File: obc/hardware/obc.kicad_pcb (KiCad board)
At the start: 4 copper layers, 80 x 80 mm, 88 parts, among them J1 Conn_ARM_JTAG_SWD_10, J2 Micro_SD_Card, J3 Conn_Coaxial, J4 USB_C_Receptacle_USB2.0_16P, J5 Conn_Coaxial, SW1 SW_SPDT, SW2 SW_Push, U1 STM32H743ZGT6, U10 LM66100DCK, U11 LM66100DCK, U12 LM66100DCK, U13 LSM6DSM, U2 RFM96W-433S2, U3 MAX6369, U4 MAX-M10S, U5 FM24CL16B, U6 MS5607-02BA, U7 SN65HVD230, U8 SN65HVD230, U9 AMS1117-3.3, Y1 25 MHz, Y2 32.768 kHz

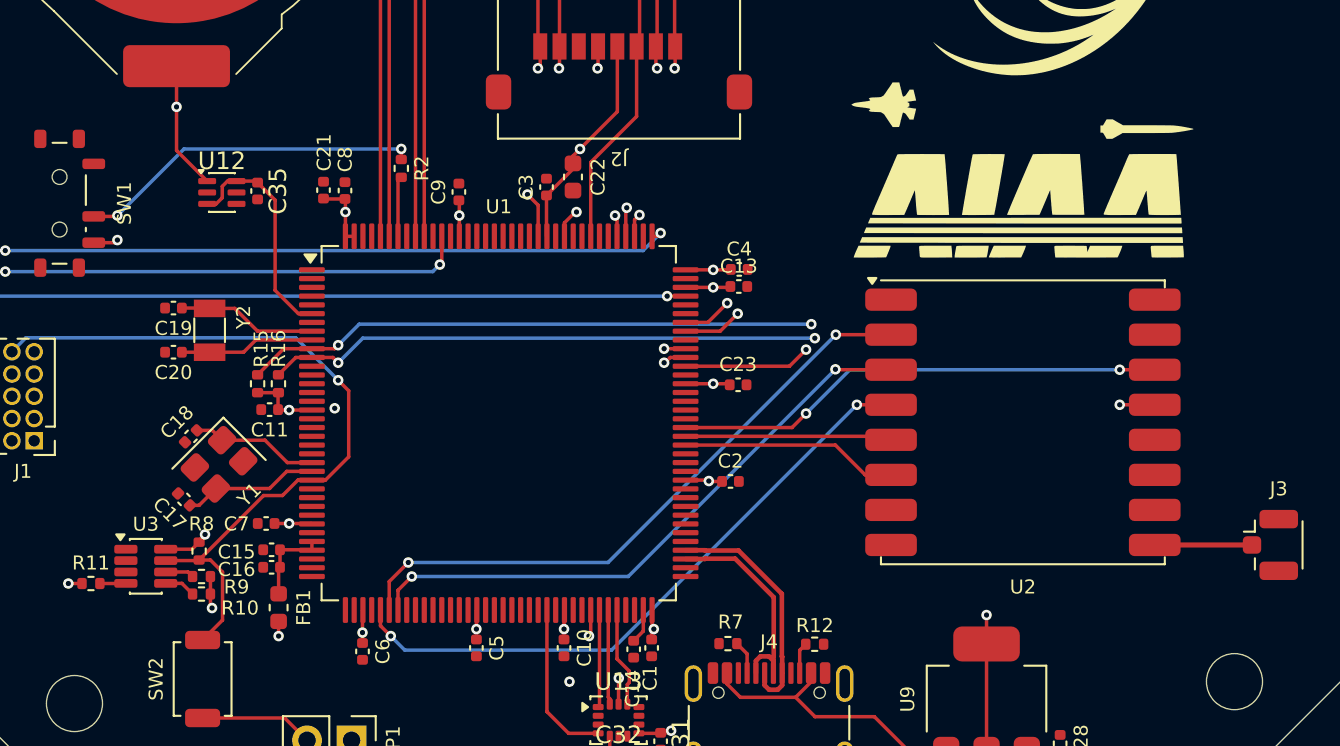
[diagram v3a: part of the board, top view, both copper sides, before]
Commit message: schematic cleanup, move to schottky diode for VBAT
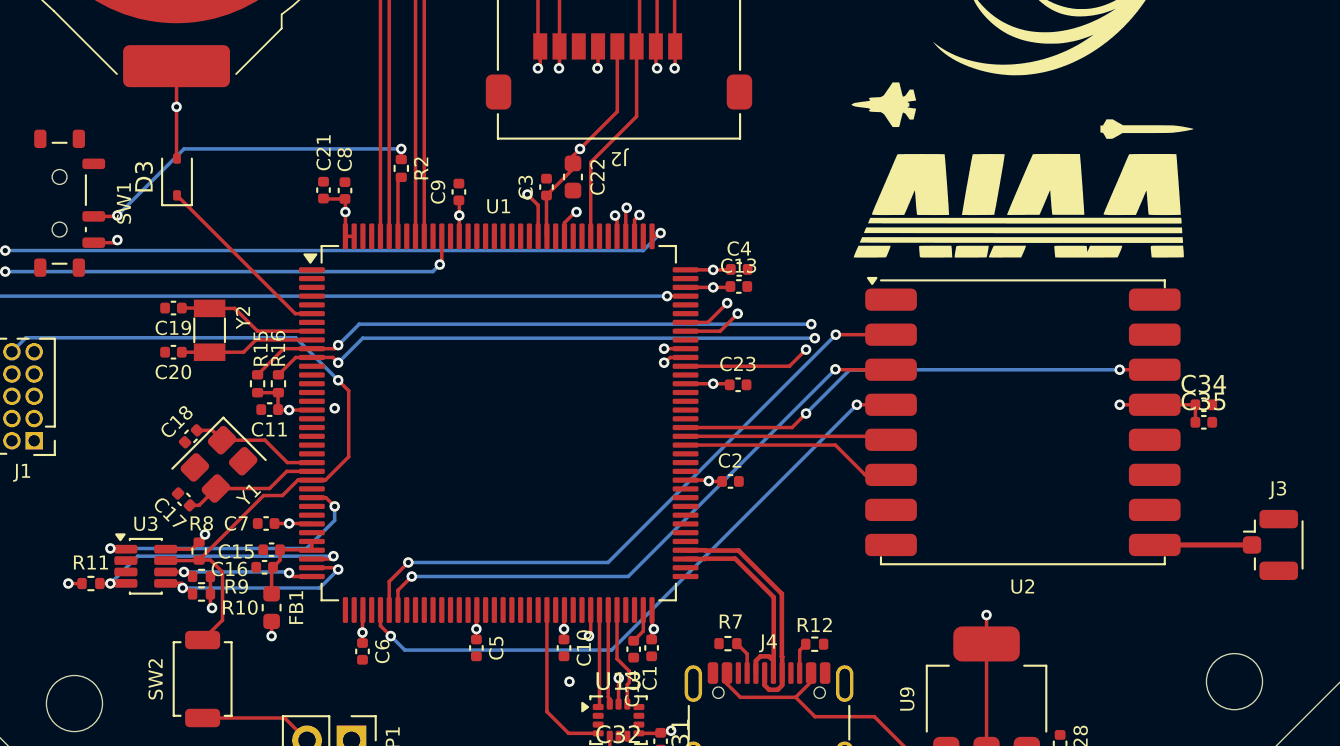
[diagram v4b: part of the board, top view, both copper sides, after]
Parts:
- removed U12: LM66100DCK, Package_TO_SOT_SMD:SOT-363_SC-70-6
- added C34: 100nF, Capacitor_SMD:C_0402_1005Metric, F.Cu at (162.8, 109.2)
- added D3: 1N5819WS, Diode_SMD:D_SOD-323, F.Cu at (104.2, 96.2)
- BT1: value Battery_Cell -> CR2032
- C35: value 100nF -> 1uF
- moved C35 55.6 mm to (162.8, 110.2), turned to 0 degrees
- moved FB1 0.40 mm to (109.6, 120.8)
- moved C16 0.40 mm to (109.2, 118.5)
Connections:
- net /STM32H7/CAN1_RX renamed /STM32H7/CAN/CAN1_RX
- net /STM32H7/CAN1_TX renamed /STM32H7/CAN/CAN1_TX
- net /STM32H7/CAN2_RX renamed /STM32H7/CAN/CAN2_RX
- net /STM32H7/CAN2_TX renamed /STM32H7/CAN/CAN2_TX
- net Net-(U1-PC14) renamed /STM32H7/RTC_I
- net Net-(U1-PC15) renamed /STM32H7/RTC_O
- C35 pad 1: Net-(U1-VBAT) -> VDD_RADIO
- U1 pad 27: unconnected-(U1-PC1-Pad27) -> /STM32H7/WDI
- U1 pad 34: unconnected-(U1-PA0-Pad34) -> /STM32H7/WD_S0
- U1 pad 35: unconnected-(U1-PA1-Pad35) -> /STM32H7/WD_S1
- U1 pad 36: unconnected-(U1-PA2-Pad36) -> /STM32H7/WD_S2
- U1 pad 6: Net-(U1-VBAT) -> Net-(D3-K)
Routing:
- net /STM32H7/WDI: track 0.00 -> 16.7 mm, vias 0 -> 2
- net /STM32H7/WD_S0: track 1.49 -> 16.2 mm, vias 0 -> 2
- net Net-(U1-VBAT): track 13.0 -> 0.00 mm
- net /STM32H7/WD_S1: track 1.78 -> 12.8 mm, vias 0 -> 2
- net Net-(D3-K): track 0.00 -> 10.5 mm
- net /STM32H7/WD_S2: track 1.64 -> 9.05 mm, vias 0 -> 2
- net VDD_RADIO: track 100.6 -> 103.9 mm
- net Net-(BT1-+): track 36.3 -> 34.3 mm

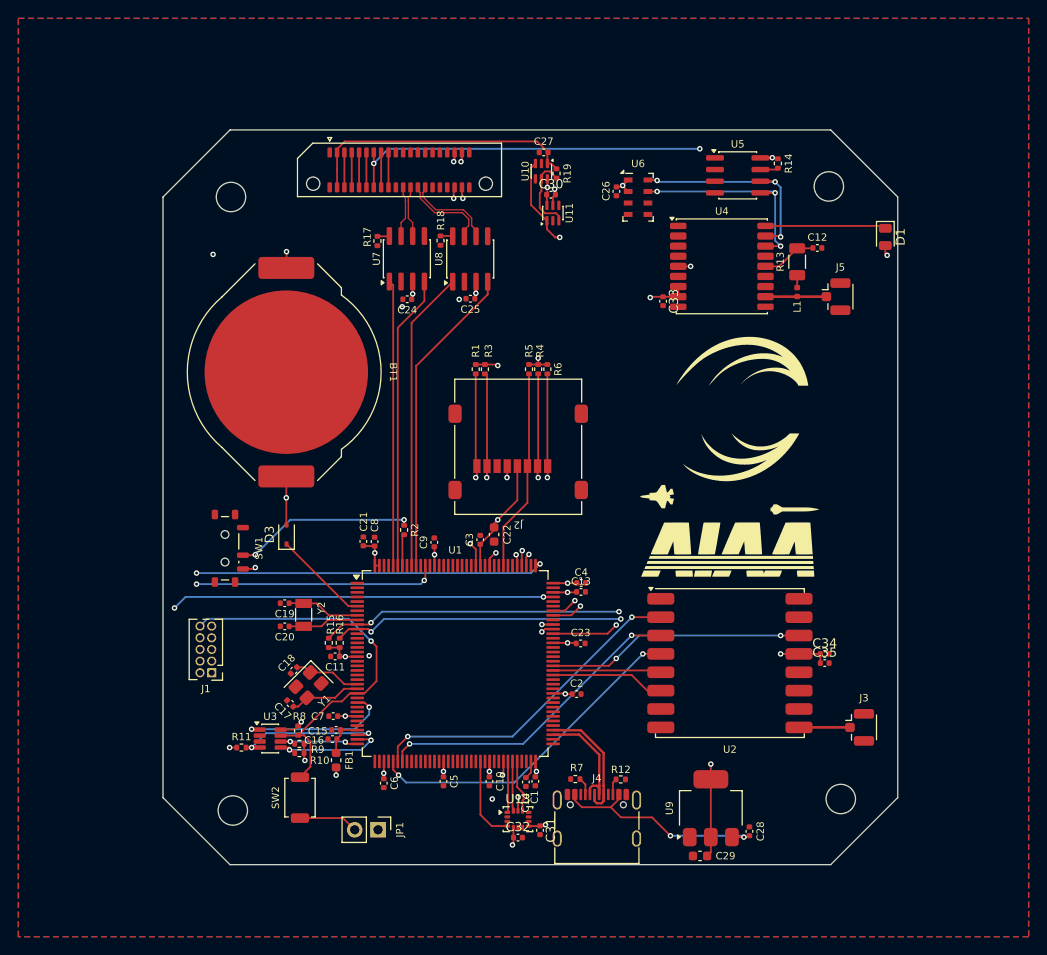
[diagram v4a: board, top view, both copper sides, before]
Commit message: add antenna supervisor, ESD, reroute some stuff
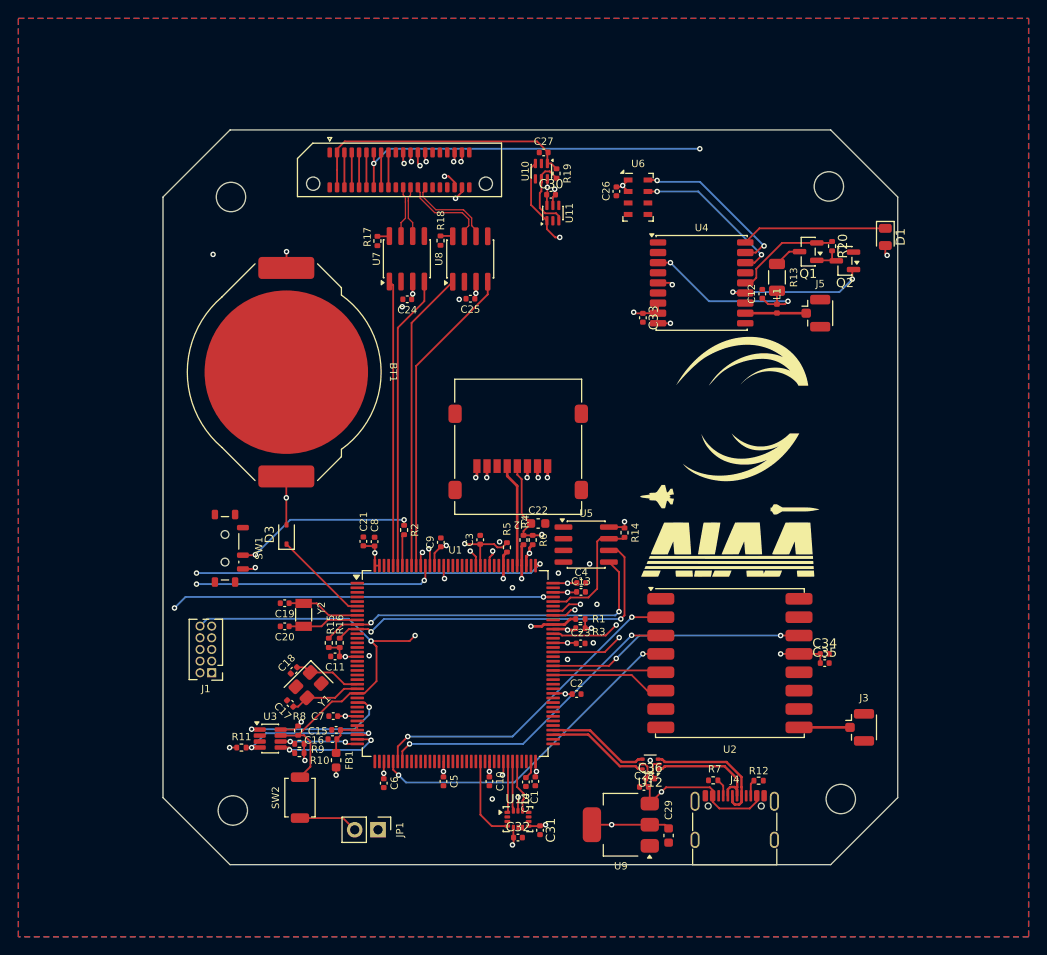
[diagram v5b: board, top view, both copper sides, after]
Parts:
- added C36: 100nF, Capacitor_SMD:C_0402_1005Metric, F.Cu at (143.8, 122.8)
- added Q1: AO3401A, Package_TO_SOT_SMD:SOT-23, F.Cu at (161.0, 65.4)
- added Q2: AO3400A, Package_TO_SOT_SMD:SOT-23, F.Cu at (165.0, 66.4)
- added R20: 51k, Resistor_SMD:R_0402_1005Metric, F.Cu at (163.6, 64.8)
- added U12: USBLC6-2P6, Package_TO_SOT_SMD:SOT-666, F.Cu at (143.8, 121.2)
- U13: value LSM6DSM -> ISM6HG256X
- moved R14 43.5 mm to (141.0, 96.0)
- moved U5 43.5 mm to (136.8, 97.3)
- moved R3 30.1 mm to (136.2, 106.4), turned to 180 degrees
- moved R1 29.5 mm to (136.2, 105.4), turned to 180 degrees
- moved R5 19.5 mm to (128.2, 97.6)
- moved R4 18.7 mm to (130.0, 96.8)
- moved R6 18.7 mm to (131.0, 96.8)
- moved J4 15.0 mm to (153.0, 128.4)
- moved R12 15.0 mm to (155.6, 123.0)
- moved R7 15.0 mm to (150.7, 123.0)
- moved C28 12.5 mm to (143.1, 123.7), turned to 180 degrees
- moved U9 9.96 mm to (140.6, 127.8), turned to 180 degrees
- moved C12 7.81 mm to (156.0, 70.0), turned to 90 degrees
- moved C22 4.95 mm to (131.6, 95.0), turned to 0 degrees
- moved C29 4.08 mm to (145.8, 129.0), turned to -90 degrees
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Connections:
- net Net-(U9-VI) renamed VBUS
- C12 pad 1: Net-(U4-VCC_RF) -> /STM32H7/Sensors/~{ANT_SHORT}
- J1 pad 10: /STM32H7/NRST -> /STM32H7/~{RESET}
- J10 pad 23: /Inter-Board-Connector/EPS_OBC_RESET -> /STM32H7/~{RESET}
- J2 pad 6: unconnected-(J2-VSS-Pad6) -> GND
- J4 pad A6: /STM32H7/USB_D+ -> /UNPROT_USB_D+
- J4 pad A7: /STM32H7/USB_D- -> /UNPROT_USB_D-
- J4 pad B6: /STM32H7/USB_D+ -> /UNPROT_USB_D+
- J4 pad B7: /STM32H7/USB_D- -> /UNPROT_USB_D-
- J5 pad 1: /STM32H7/Sensors/GPS_ANT -> /STM32H7/Sensors/GNSS_ANT
- L1 pad 1: Net-(L1-Pad1) -> /STM32H7/Sensors/GNSS_ANT
- L1 pad 2: /STM32H7/Sensors/GPS_ANT -> /STM32H7/Sensors/~{ANT_SHORT}
- R13 pad 1: Net-(L1-Pad1) -> Net-(Q1-D)
- R13 pad 2: Net-(U4-VCC_RF) -> /STM32H7/Sensors/~{ANT_SHORT}
- R8 pad 2: /STM32H7/NRST -> /STM32H7/~{RESET}
- SW2 pad 2: /STM32H7/NRST -> /STM32H7/~{RESET}
- U1 pad 101: /Inter-Board-Connector/SYSTEM_MAIN_UART_TX -> /Inter-Board-Connector/SYSTEM_MAIN_UART_RX
- U1 pad 102: /Inter-Board-Connector/SYSTEM_MAIN_UART_RX -> /Inter-Board-Connector/SYSTEM_MAIN_UART_TX
- U1 pad 104: unconnected-(U1-PA12-Pad104) -> /STM32H7/FRAM_WP
- U1 pad 119: /Inter-Board-Connector/SYSTEM_AUX_UART_TX -> /Inter-Board-Connector/SYSTEM_AUX_UART_RX
- U1 pad 122: /Inter-Board-Connector/SYSTEM_AUX_UART_RX -> /Inter-Board-Connector/SYSTEM_AUX_UART_TX
- U1 pad 129: unconnected-(U1-PG14-Pad129) -> /Inter-Board-Connector/EPS_PGOOD
- U1 pad 132: unconnected-(U1-PG15-Pad132) -> /Inter-Board-Connector/OBC_HEARTBEAT
- U1 pad 134: unconnected-(U1-PB4-Pad134) -> /Inter-Board-Connector/OBC_EPS_RESET
- U1 pad 25: /STM32H7/NRST -> /STM32H7/~{RESET}
- U1 pad 93: unconnected-(U1-PG8-Pad93) -> /STM32H7/~{GPS_RESET}
- U3 pad 7: /STM32H7/NRST -> /STM32H7/~{RESET}
- U4 pad 11: /STM32H7/Sensors/GPS_ANT -> /STM32H7/Sensors/GNSS_ANT
- U4 pad 13: unconnected-(U4-LNA_EN-Pad13) -> Net-(Q2-G)
- U4 pad 14: Net-(U4-VCC_RF) -> Net-(Q1-S)
- U4 pad 3: unconnected-(U4-RXD-Pad3) -> /STM32H7/Sensors/~{ANT_SHORT}
- U4 pad 9: unconnected-(U4-~{RESET}-Pad9) -> /STM32H7/~{GPS_RESET}
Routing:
- net /STM32H7/~{RESET}: track 0.00 -> 101.6 mm, vias 0 -> 3
- net /STM32H7/~{GPS_RESET}: track 0.00 -> 59.0 mm, vias 0 -> 2
- net /Inter-Board-Connector/EPS_PGOOD: track 0.00 -> 52.7 mm, vias 0 -> 2
- net /Inter-Board-Connector/OBC_EPS_RESET: track 0.00 -> 45.3 mm, vias 0 -> 2
- net /Inter-Board-Connector/OBC_HEARTBEAT: track 0.00 -> 45.2 mm, vias 0 -> 2
- net /STM32H7/NRST: track 43.4 -> 0.00 mm, vias 1 -> 0
- net /STM32H7/Sensors/~{ANT_SHORT}: track 0.00 -> 20.5 mm, vias 0 -> 2
- net Net-(Q2-G): track 0.00 -> 16.1 mm, vias 0 -> 2
- net /UNPROT_USB_D+: track 0.00 -> 14.6 mm
- net /UNPROT_USB_D-: track 0.00 -> 13.8 mm
- net Net-(Q1-S): track 0.00 -> 11.9 mm
- net /STM32H7/FRAM_WP: track 1.96 -> 13.7 mm
- net /STM32H7/SD_D2: track 21.8 -> 13.8 mm
- net /STM32H7/Sensors/GPS_ANT: track 6.63 -> 0.00 mm
- net /STM32H7/Sensors/GNSS_ANT: track 0.00 -> 6.63 mm
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
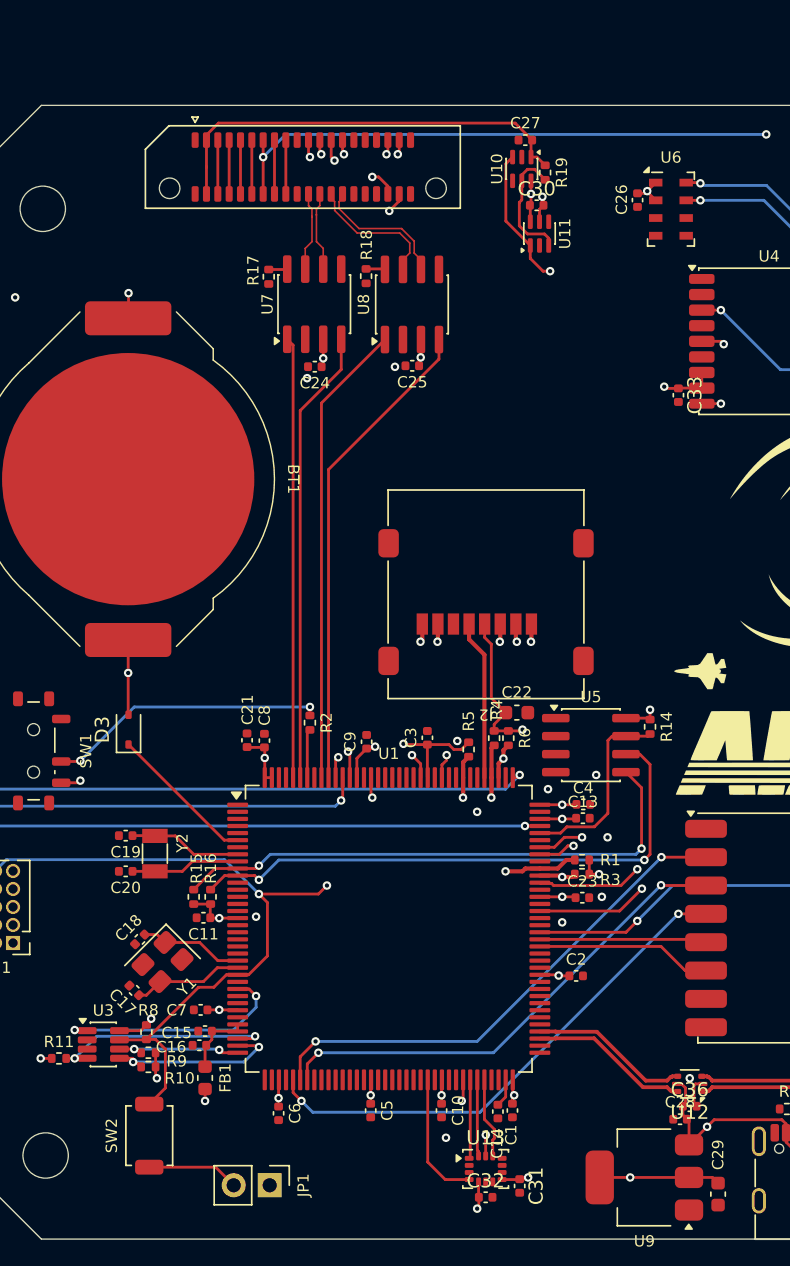
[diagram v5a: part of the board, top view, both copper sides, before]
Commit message: add TVS diodes, rotate decoupling capacitors
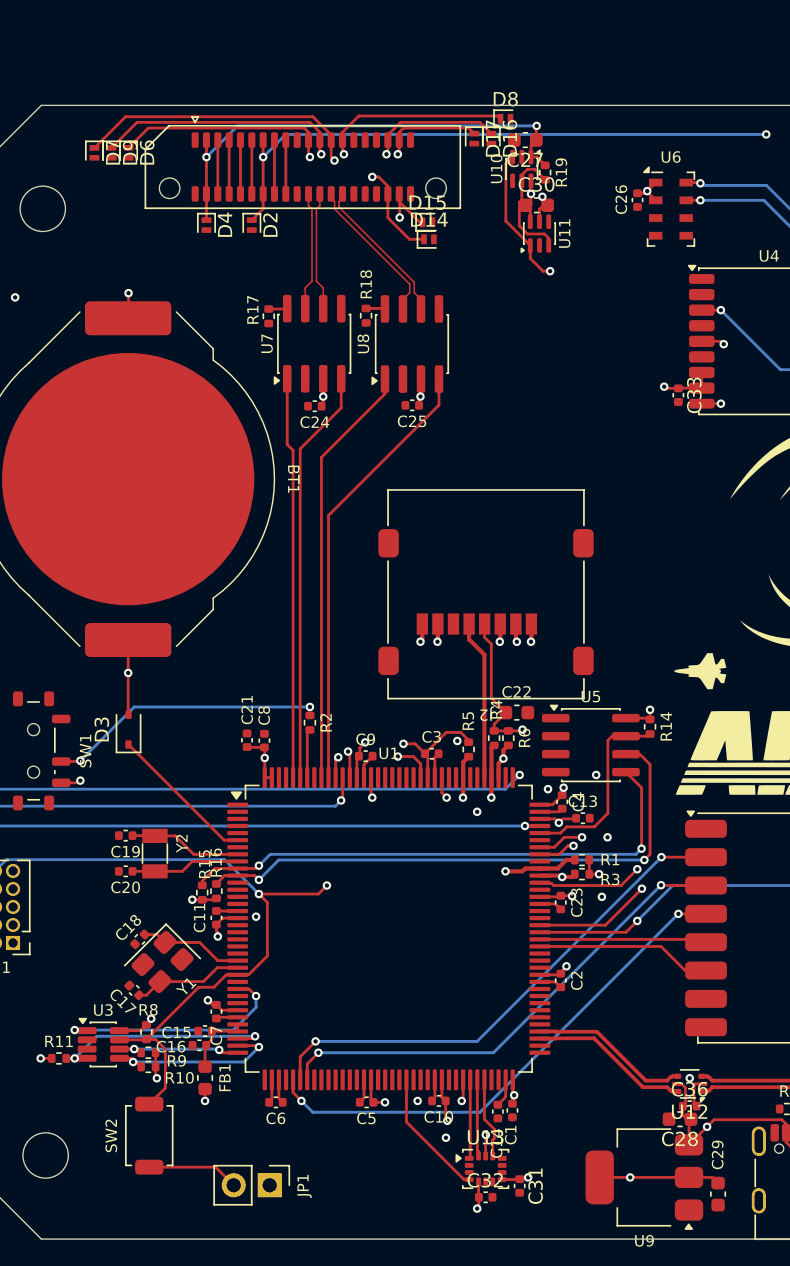
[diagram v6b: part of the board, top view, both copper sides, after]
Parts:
- added D14: D_Zener, Diode_SMD:D_SOD-882, F.Cu at (125.4, 61.6)
- added D15: D_Zener, Diode_SMD:D_SOD-882, F.Cu at (125.3, 60.4)
- added D16: D_Zener, Diode_SMD:D_SOD-882, F.Cu at (129.8, 54.5)
- added D17: D_Zener, Diode_SMD:D_SOD-882, F.Cu at (128.6, 54.5)
- added D2: D_Zener, Diode_SMD:D_SOD-882, F.Cu at (112.9, 60.6)
- added D4: D_Zener, Diode_SMD:D_SOD-882, F.Cu at (109.7, 60.6)
- added D6: D_Zener, Diode_SMD:D_SOD-882, F.Cu at (104.2, 55.5)
- added D7: D_Zener, Diode_SMD:D_SOD-882, F.Cu at (101.8, 55.5)
- added D8: D_Zener, Diode_SMD:D_SOD-882, F.Cu at (130.8, 53.1)
- added D9: D_Zener, Diode_SMD:D_SOD-882, F.Cu at (103.0, 55.5)
- C12: value 10n -> 10nF
- C21: value 4.7u -> 4.7uF
- C27, C28, C30: value 10u -> 10uF; footprint Capacitor_SMD:C_0402_1005Metric -> Capacitor_SMD:C_0603_1608Metric
- R2: value R_Small_US -> 10k
- moved C24 2.79 mm to (117.3, 73.4)
- moved C25 2.79 mm to (124.2, 73.3)
- moved R17 2.79 mm to (114.1, 67.0)
- moved R18 2.79 mm to (121.0, 67.0)
- moved U7 2.79 mm to (117.3, 69.0)
- moved U8 2.79 mm to (124.2, 69.0)
- moved C23 1.56 mm to (134.7, 108.4), turned to -90 degrees
- moved C4 1.50 mm to (134.8, 101.3), turned to -90 degrees
- moved C3 1.17 mm to (125.6, 97.9), turned to 0 degrees
- moved C2 1.14 mm to (134.7, 113.9), turned to -90 degrees
- moved C7 1.12 mm to (110.4, 116.1), turned to -90 degrees
- moved C9 1.02 mm to (120.9, 98.1), turned to 0 degrees
- moved C11 0.91 mm to (110.4, 109.5), turned to 90 degrees
- moved C6 0.80 mm to (114.6, 122.5), turned to 180 degrees
- moved C10 0.70 mm to (126.1, 122.4), turned to 180 degrees
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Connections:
- U1 pad 57: unconnected-(U1-PG1-Pad57) -> /STM32H7/IMU_INT
- U1 pad 60: /STM32H7/Sensors/IMU_INTERRUPT -> unconnected-(U1-PE9-Pad60)
- U1 pad 91: unconnected-(U1-PG6-Pad91) -> /STM32H7/~{GPS_RESET}
- U1 pad 93: /STM32H7/~{GPS_RESET} -> unconnected-(U1-PG8-Pad93)
- U13 pad 4: /STM32H7/Sensors/IMU_INTERRUPT -> /STM32H7/IMU_INT
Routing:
- net /Inter-Board-Connector/OBC_EPS_RESET: track 45.3 -> 63.8 mm
- net /STM32H7/~{RESET}: track 101.6 -> 118.4 mm
- net GND: track 4.13 -> 20.6 mm, vias 14 -> 12
- net /Inter-Board-Connector/EPS_PGOOD: track 52.7 -> 66.7 mm
- net /Inter-Board-Connector/OBC_HEARTBEAT: track 45.2 -> 57.5 mm
- net /STM32H7/Sensors/IMU_INTERRUPT: track 9.24 -> 0.00 mm
- net /STM32H7/IMU_INT: track 0.00 -> 9.08 mm
- net /Inter-Board-Connector/SYSTEM_MAIN_UART_RX: track 57.9 -> 66.3 mm
- net /Inter-Board-Connector/SYSTEM_AUX_UART_RX: track 46.6 -> 54.3 mm
- net /Inter-Board-Connector/SYSTEM_MAIN_UART_TX: track 57.9 -> 64.0 mm
- net /Inter-Board-Connector/SYSTEM_AUX_UART_TX: track 44.1 -> 47.9 mm
- net /Inter-Board-Connector/RAIL_1_VOUT: track 30.5 -> 33.5 mm, vias 0 -> 2
- net /STM32H7/CAN/CAN2_TX: track 32.8 -> 30.0 mm
- net /STM32H7/CAN/CAN2_RX: track 34.1 -> 31.4 mm
- net /STM32H7/CAN/CAN1_TX: track 31.1 -> 28.3 mm
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
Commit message: ground via spam
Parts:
- moved C30 0.33 mm to (133.2, 59.0)
- moved C27 0.15 mm to (132.2, 54.4)
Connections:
- C14 pad 1: Net-(C14-Pad1) -> Net-(C13-Pad1)
- U1 pad 71: Net-(C14-Pad1) -> Net-(C13-Pad1)
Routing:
- net Net-(C13-Pad1): track 2.80 -> 25.5 mm
- net Net-(C14-Pad1): track 1.99 -> 0.00 mm
- net +3V3: track 77.5 -> 78.9 mm, vias 28 -> 29
- net SCL: track 107.9 -> 108.8 mm
- net /STM32H7/SWDIO: track 49.9 -> 49.1 mm
- net GND: track 20.6 -> 21.1 mm, vias 12 -> 808
